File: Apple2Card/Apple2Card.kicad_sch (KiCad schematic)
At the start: 55 parts, among them J1 ICSP, J2 Conn_01x25, J3 Conn_01x25, J4 Conn_01x16, J5 Conn_01x04, J6 WIZNET 5500, J7 Conn_01x04, SW1 SW_Push, U1 ATmega328P-P, U3 74HCT00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

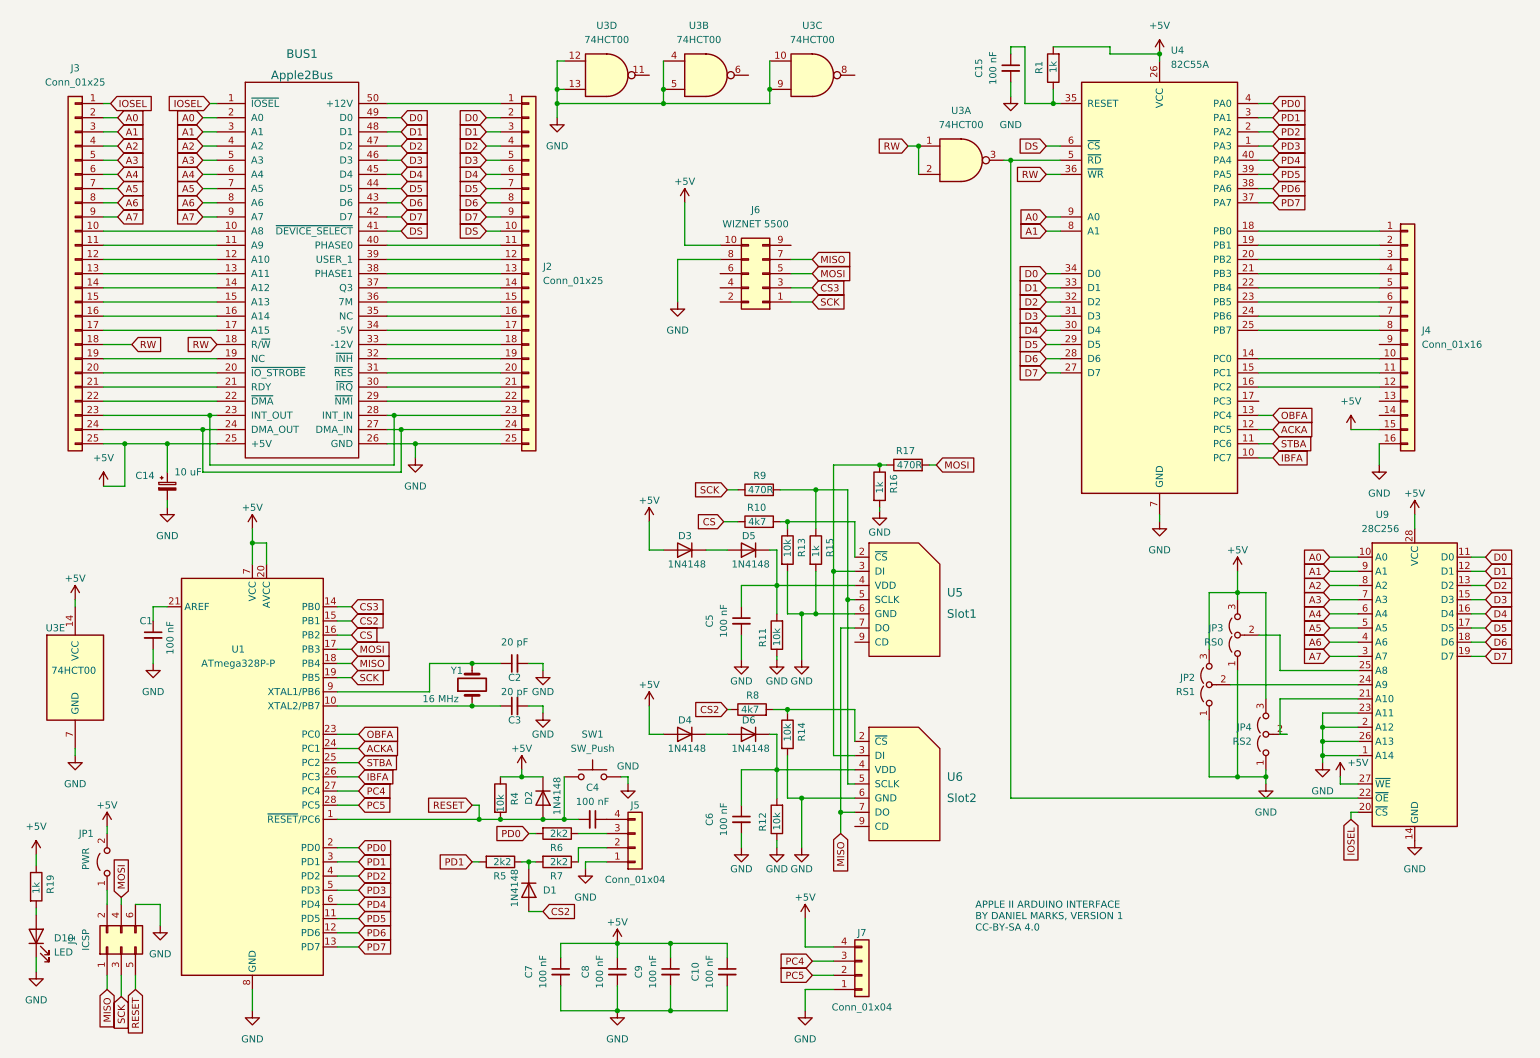
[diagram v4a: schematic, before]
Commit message: Added ROM banking
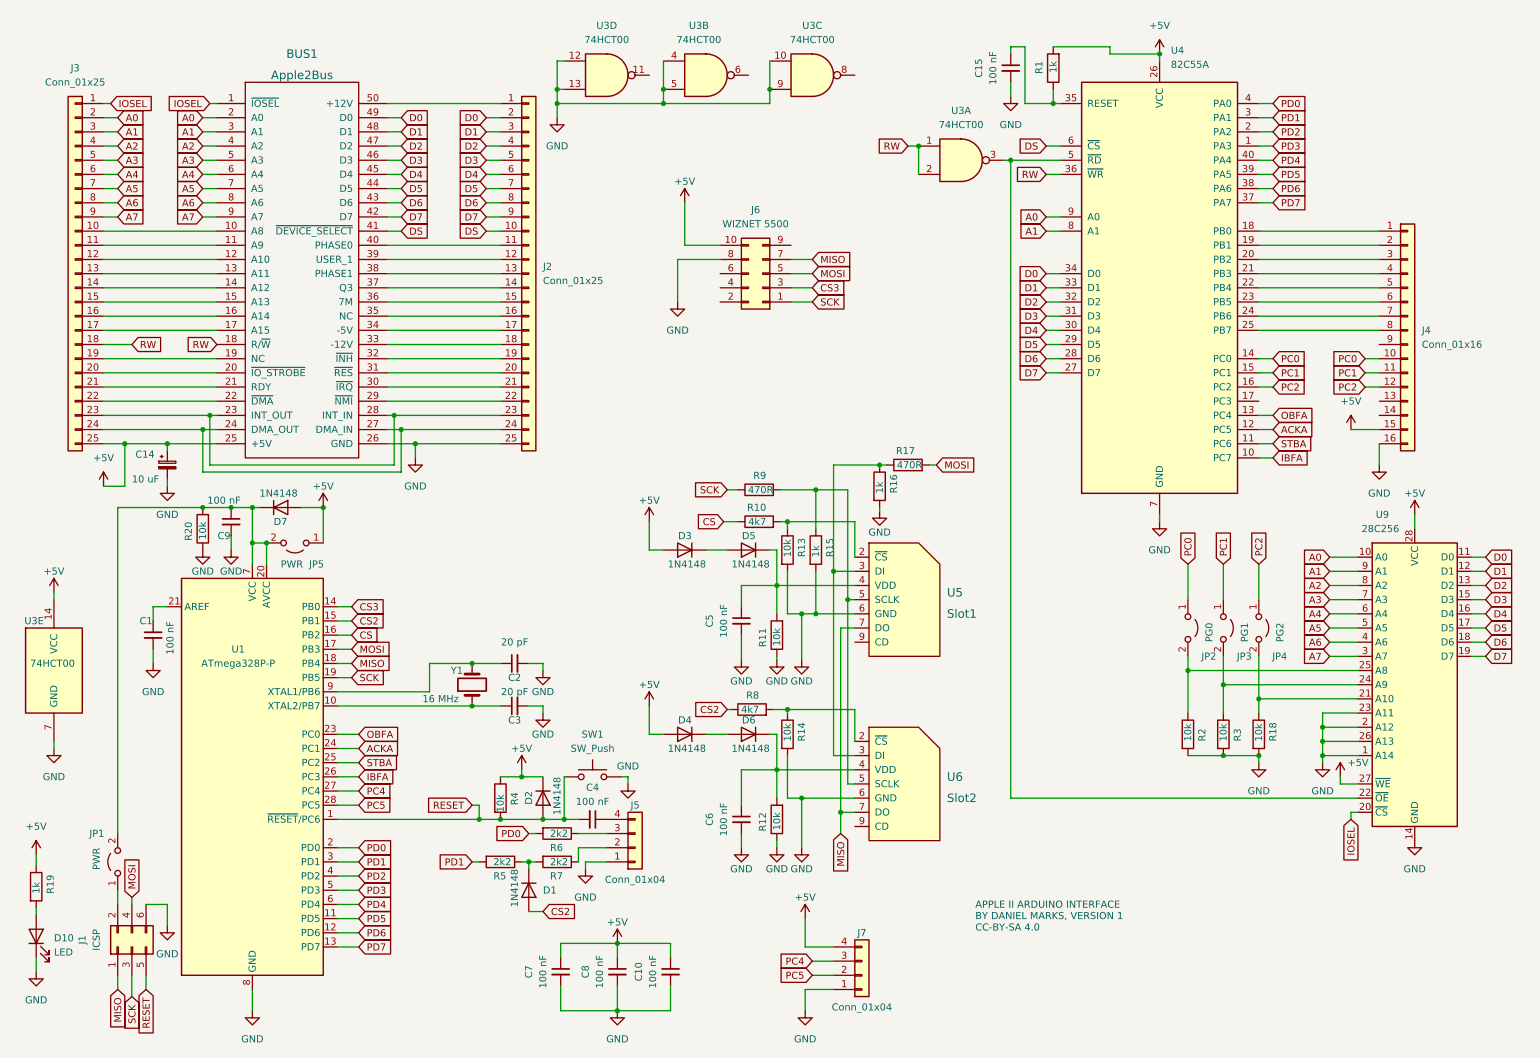
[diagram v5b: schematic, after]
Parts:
- removed JP2: RS1, Connector_PinHeader_2.54mm:PinHeader_1x03_P2.54mm_Vertical, symbol Jumper:Jumper_3_Open
- removed JP3: RS0, Connector_PinHeader_2.54mm:PinHeader_1x03_P2.54mm_Vertical, symbol Jumper:Jumper_3_Open
- removed JP4: RS2, Connector_PinHeader_2.54mm:PinHeader_1x03_P2.54mm_Vertical, symbol Jumper:Jumper_3_Open
- added D7: 1N4148, Diode_THT:D_DO-35_SOD27_P7.62mm_Horizontal, symbol Device:D
- added JP2: PG0, Connector_PinHeader_2.54mm:PinHeader_1x02_P2.54mm_Vertical, symbol Jumper:Jumper_2_Open
- added JP3: PG1, Connector_PinHeader_2.54mm:PinHeader_1x02_P2.54mm_Vertical, symbol Jumper:Jumper_2_Open
- added JP4: PG2, Connector_PinHeader_2.54mm:PinHeader_1x02_P2.54mm_Vertical, symbol Jumper:Jumper_2_Open
- added JP5: PWR, Connector_PinHeader_2.54mm:PinHeader_1x02_P2.54mm_Vertical, symbol Jumper:Jumper_2_Open
- added R18, R2, R20, R3: 10k, Resistor_THT:R_Axial_DIN0207_L6.3mm_D2.5mm_P7.62mm_Horizontal, symbol Device:R
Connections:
- net +5V: now also D7.2 (A), JP5.1 (A); no longer C9.1, JP1.2 (B), U1.20 (AVCC), U1.7 (VCC)
- net GND: now also R18.2, R2.2, R20.1, R3.2
- net at U9.21 (A10): now also JP4.2 (B), R18.1
- net at U9.24 (A9): now also JP3.2 (B), R3.1
- net at U9.25 (A8): now also JP2.2 (B), R2.1
- net PC0: now reaches J4.10 (Pin_10), U4.14 (PC0)
- net PC0: now also JP2.1 (A)
- net PC1: now reaches J4.11 (Pin_11), U4.15 (PC1)
- net PC1: now also JP3.1 (A)
- net PC2: now reaches J4.12 (Pin_12), U4.16 (PC2)
- net PC2: now also JP4.1 (A)
- new net: C9.1, D7.1 (K), JP1.2 (B), JP5.2 (B), R20.2, U1.20 (AVCC), U1.7 (VCC)
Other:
- moved on the sheet: C10, C14, C9, J1, JP1, U3E

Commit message: Added initial boot firmware
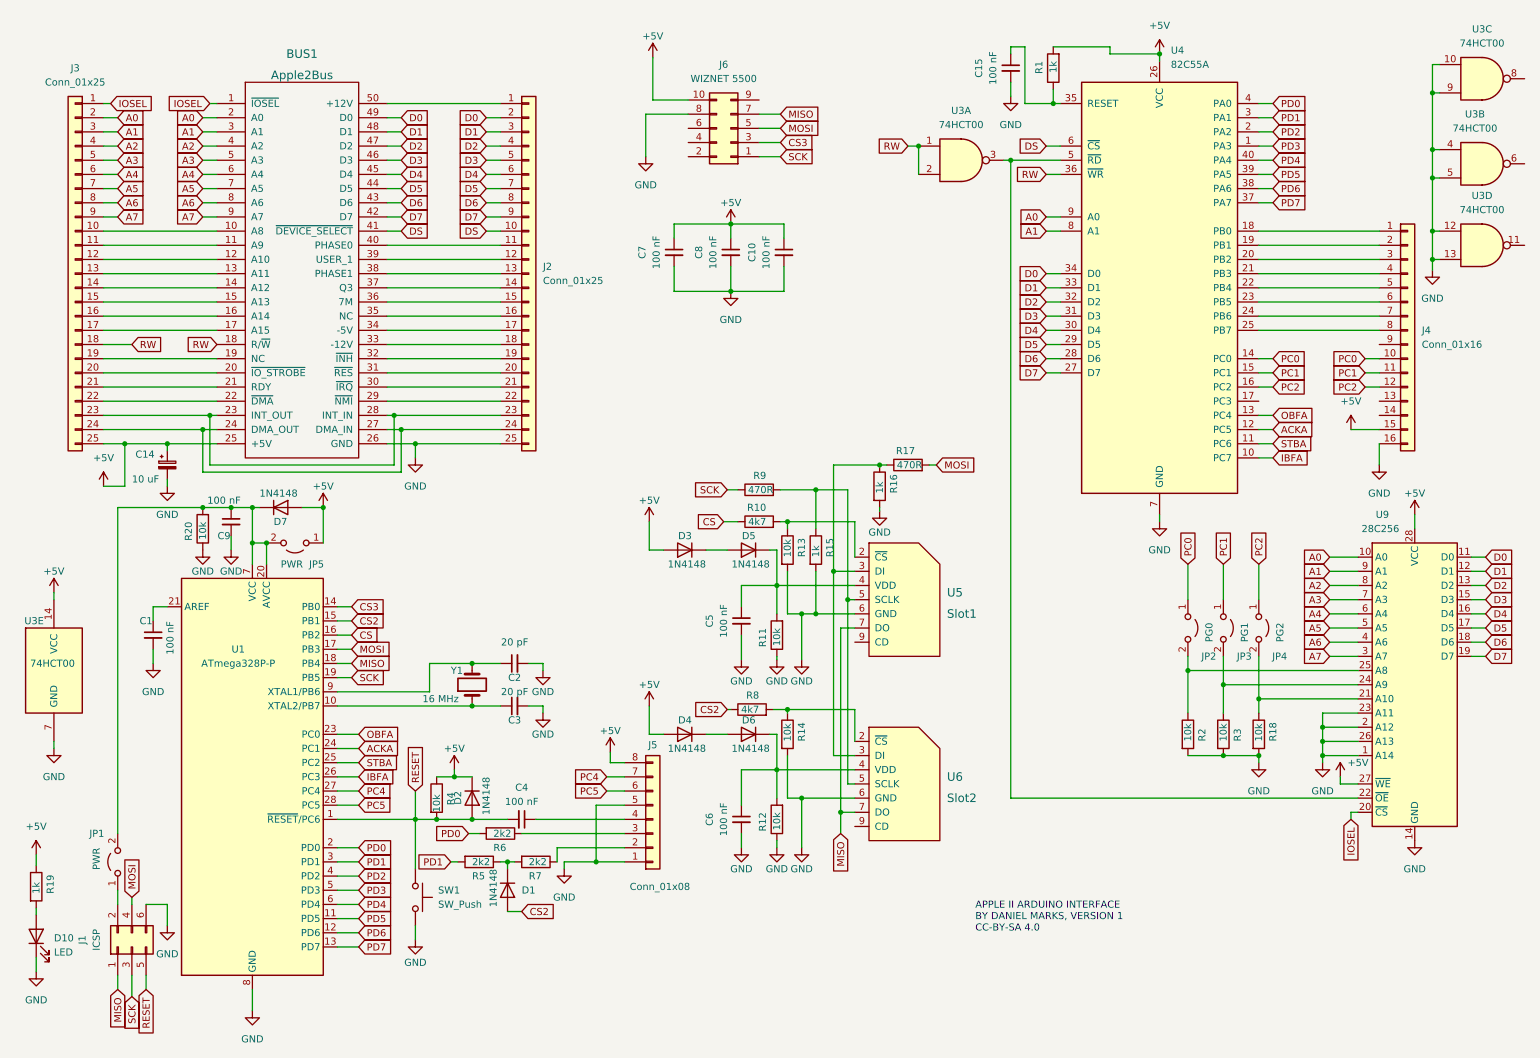
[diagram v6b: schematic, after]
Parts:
- removed J5, J7: Conn_01x04, Connector_PinHeader_2.54mm:PinHeader_1x04_P2.54mm_Vertical, symbol Connector_Generic:Conn_01x04
- added J5: Conn_01x08, Connector_PinHeader_2.54mm:PinHeader_1x08_P2.54mm_Vertical, symbol Connector_Generic:Conn_01x08
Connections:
- net +5V: now also J5.8 (Pin_8)
- net GND: now also J5.1 (Pin_1), J5.5 (Pin_5)
- net PC4: now also J5.7 (Pin_7)
- net PC5: now also J5.6 (Pin_6)
- net at R7.1: now also J5.2 (Pin_2)
- net at R6.1: now also J5.3 (Pin_3)
- net at C4.1: now also J5.4 (Pin_4)
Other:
- moved on the sheet: C10, C4, C7, C8, D1, D2, J6, R4, R5, R6, R7, SW1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

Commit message: Fixed reset circuitry
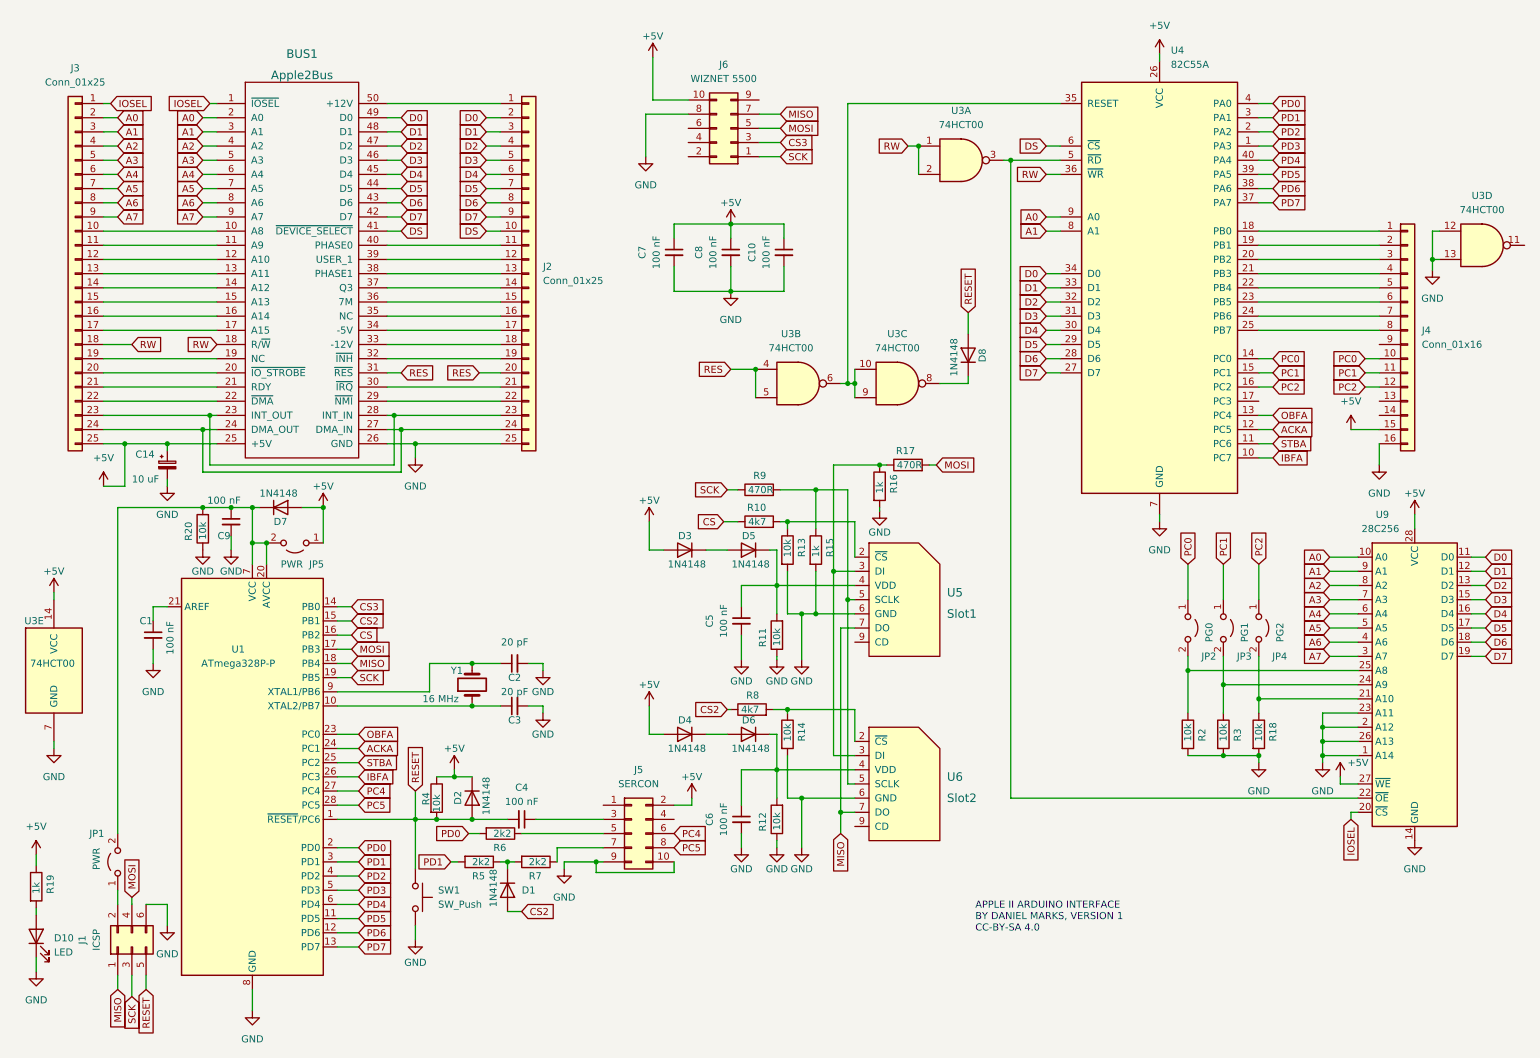
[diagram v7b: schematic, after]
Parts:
- removed C15: 100 nF, Capacitor_THT:C_Disc_D5.0mm_W2.5mm_P5.00mm, symbol Device:C_Small
- removed J5: Conn_01x08, Connector_PinHeader_2.54mm:PinHeader_1x08_P2.54mm_Vertical, symbol Connector_Generic:Conn_01x08
- removed R1: 1k, Resistor_THT:R_Axial_DIN0207_L6.3mm_D2.5mm_P7.62mm_Horizontal, symbol Device:R
- added D8: 1N4148, Diode_THT:D_DO-35_SOD27_P7.62mm_Horizontal, symbol Device:D
- added J5: SERCON, Connector_PinHeader_2.54mm:PinHeader_2x05_P2.54mm_Vertical, symbol Connector_Generic:Conn_02x05_Odd_Even
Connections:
- net +5V: now also J5.2 (Pin_2)
- net GND: now also J5.10 (Pin_10), J5.9 (Pin_9); no longer U3.10, U3.4, U3.5, U3.9
- net PC4: now also J5.6 (Pin_6)
- net PC5: now also J5.8 (Pin_8)
- net RESET: now also D8.2 (A)
- net at U3.6: now also U3.10, U3.9, U4.35 (RESET)
- net at R7.1: now also J5.7 (Pin_7)
- net at R6.1: now also J5.5 (Pin_5)
- net at C4.1: now also J5.3 (Pin_3)
- net RES: now reaches BUS1.31 (~{RES}), J2.20 (Pin_20)
- net RES: now also U3.4, U3.5
- net at U3.8: now also D8.1 (K)
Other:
- moved on the sheet: U3B, U3C
